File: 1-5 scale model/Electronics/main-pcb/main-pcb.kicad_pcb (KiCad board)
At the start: 2 copper layers, 57 x 89 mm, 21 parts

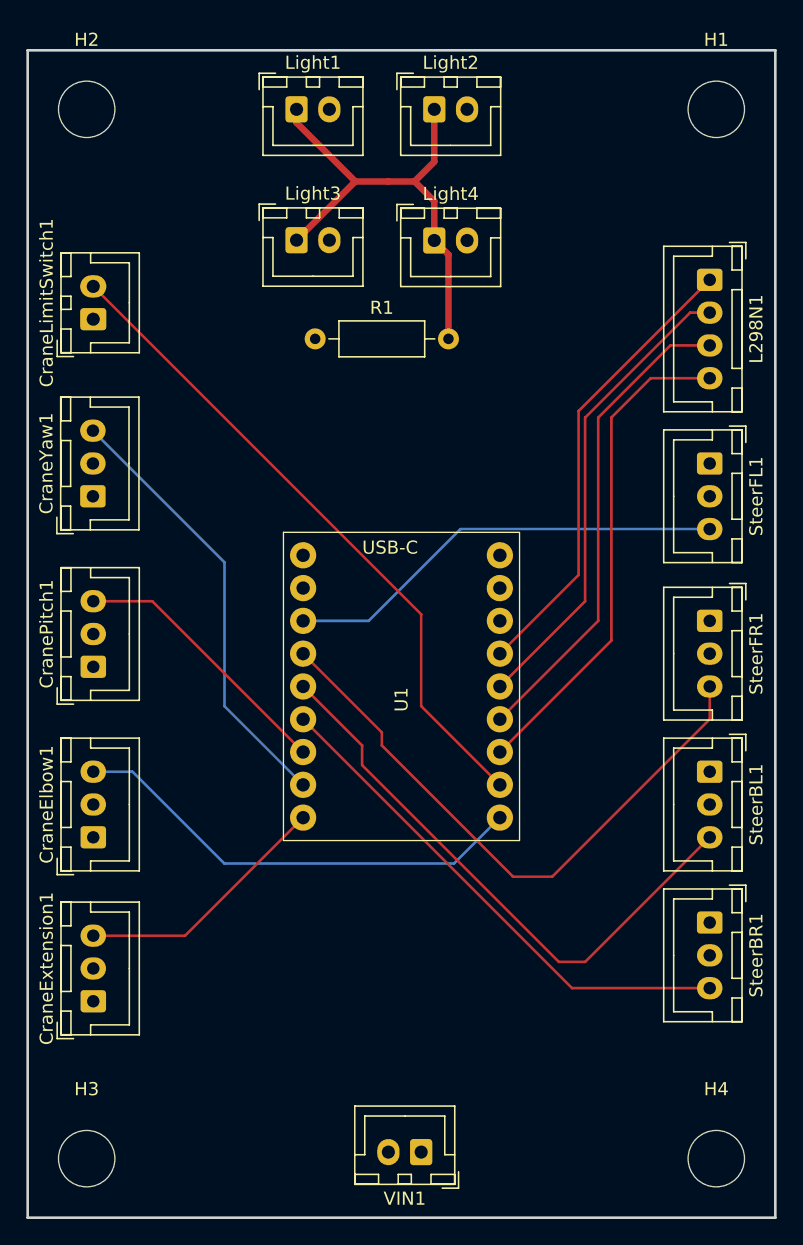
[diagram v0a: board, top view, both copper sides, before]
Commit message: updated pitch motor
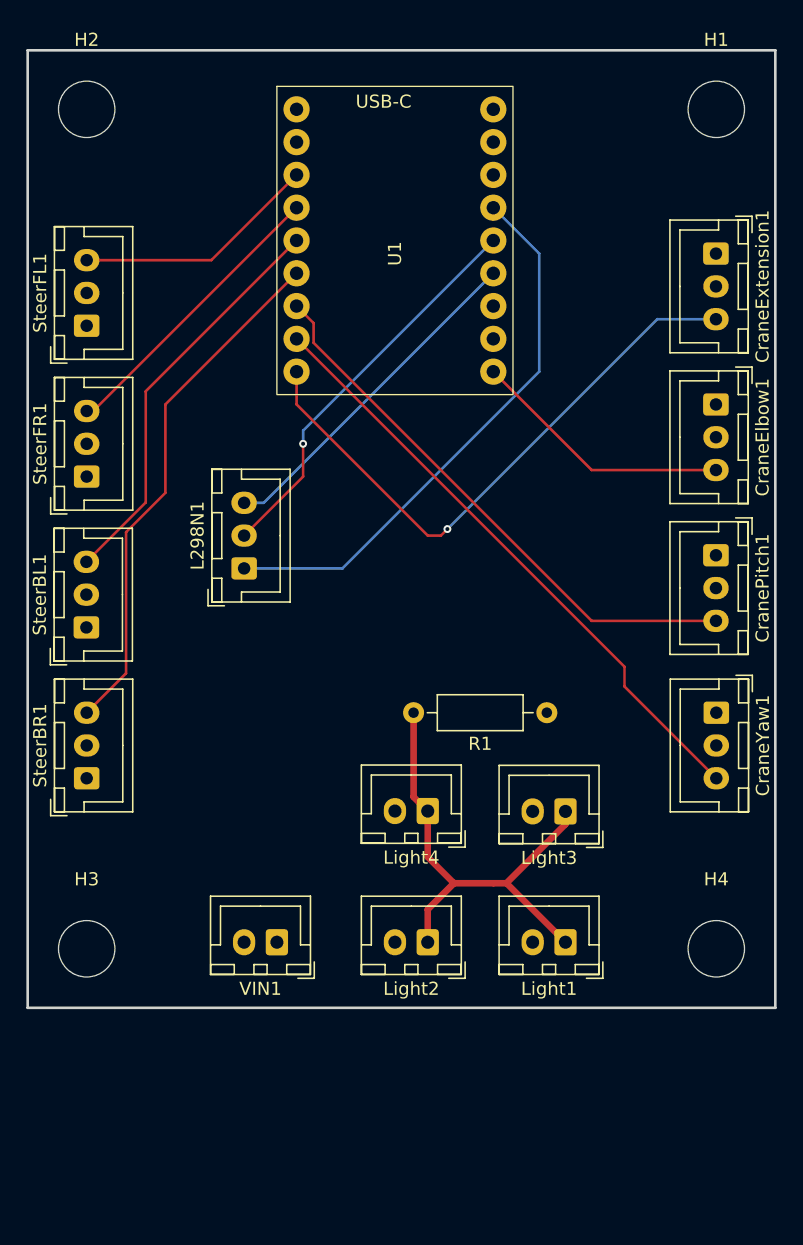
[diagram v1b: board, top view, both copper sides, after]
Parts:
- removed CraneLimitSwitch1: Crane Limit Switch, Connector_JST:JST_XH_B2B-XH-A_1x02_P2.50mm_Vertical
- L298N1: footprint Connector_JST:JST_XH_B4B-XH-A_1x04_P2.50mm_Vertical -> Connector_JST:JST_XH_B3B-XH-A_1x03_P2.50mm_Vertical
- moved CraneExtension1 74.2 mm to (170.0, 72.5), turned to -90 degrees
- moved Light1 66.7 mm to (158.5, 125.0), turned to 180 degrees
- moved Light2 63.5 mm to (148.0, 125.0), turned to 180 degrees
- moved CraneElbow1 57.8 mm to (170.0, 84.0), turned to -90 degrees
- moved CraneYaw1 50.3 mm to (170.0, 107.5), turned to -90 degrees
- moved SteerBL1 48.8 mm to (122.0, 101.0), turned to 90 degrees
- moved SteerBR1 48.8 mm to (122.0, 112.5), turned to 90 degrees
- moved SteerFR1 48.8 mm to (122.0, 89.5), turned to 90 degrees
- moved SteerFL1 48.6 mm to (122.0, 78.0), turned to 90 degrees
- moved CranePitch1 48.2 mm to (170.0, 95.5), turned to -90 degrees
- moved Light3 48.1 mm to (158.5, 115.0), turned to 180 degrees
- moved Light4 43.5 mm to (148.0, 115.0), turned to 180 degrees
- moved L298N1 41.8 mm to (134.0, 96.5), turned to 90 degrees
- moved U1 34.0 mm to (145.5, 71.5)
- moved R1 33.5 mm to (157.1, 107.5), turned to 180 degrees
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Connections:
- net L298N_IN3 renamed L298N_ENA
- U1 pad 10: L298N_IN4 -> unconnected-(U1-GP10-Pad10)
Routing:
- net Crane_Limit_Switch: track 50.8 -> 0.00 mm
- net L298N_IN4: track 37.8 -> 0.00 mm
- net Crane_Servo_Extension: track 19.7 -> 45.5 mm, vias 0 -> 1
- net Signal_Steer_Servo_Front_Right: track 46.1 -> 22.4 mm
- net Crane_Servo_Pitch: track 20.8 -> 42.8 mm
- net Crane_Servo_Elbow: track 35.3 -> 20.1 mm
- net Signal_Steer_Servo_Front_Left: track 33.9 -> 18.7 mm
- net Signal_Steer_Servo_Back_Left: track 44.5 -> 31.1 mm
- net Crane_Servo_Yaw: track 33.6 -> 46.8 mm
- net L298N_ENA: track 36.9 -> 26.2 mm
- net L298N_IN1: track 35.1 -> 42.7 mm
- net L298N_IN2: track 36.0 -> 30.4 mm, vias 0 -> 1
- net Signal_Steer_Servo_Back_Right: track 39.5 -> 40.1 mm
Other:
- board size 57 x 89 mm -> 57 x 73 mm

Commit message: added battery voltage detector
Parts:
- added 10K: 18000, Resistor_THT:R_Axial_DIN0207_L6.3mm_D2.5mm_P10.16mm_Horizontal, F.Cu at (142.7, 107.5)
- added 18K: 10000, Resistor_THT:R_Axial_DIN0207_L6.3mm_D2.5mm_P10.16mm_Horizontal, F.Cu at (132.4, 103.0)
- added Battery1: Battery, Connector_JST:JST_XH_B2B-XH-A_1x02_P2.50mm_Vertical, F.Cu at (136.5, 115.0)
- Light Resistor: renamed from R1
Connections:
- U1 pad 9: Crane_Limit_Switch -> Battery_Voltage_Measure
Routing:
- net Battery_Voltage_Measure: track 0.00 -> 37.1 mm, vias 0 -> 1
- net Net-(Battery1-Pin_2): track 0.00 -> 11.8 mm
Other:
- board text added: "ENA IN1 IN2"
- board text added: "GND +5V"
- board text added: "GND +5V Sig"
- board text added: "GND PWR"
- board text added: "Sig +5V GND"
